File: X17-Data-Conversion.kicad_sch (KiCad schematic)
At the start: 18 parts, among them J1 Conn_01x05, SW1 1825910-6, U1 ABLS-8.000MHZ-B2-T, U2 STM32F091CCTx

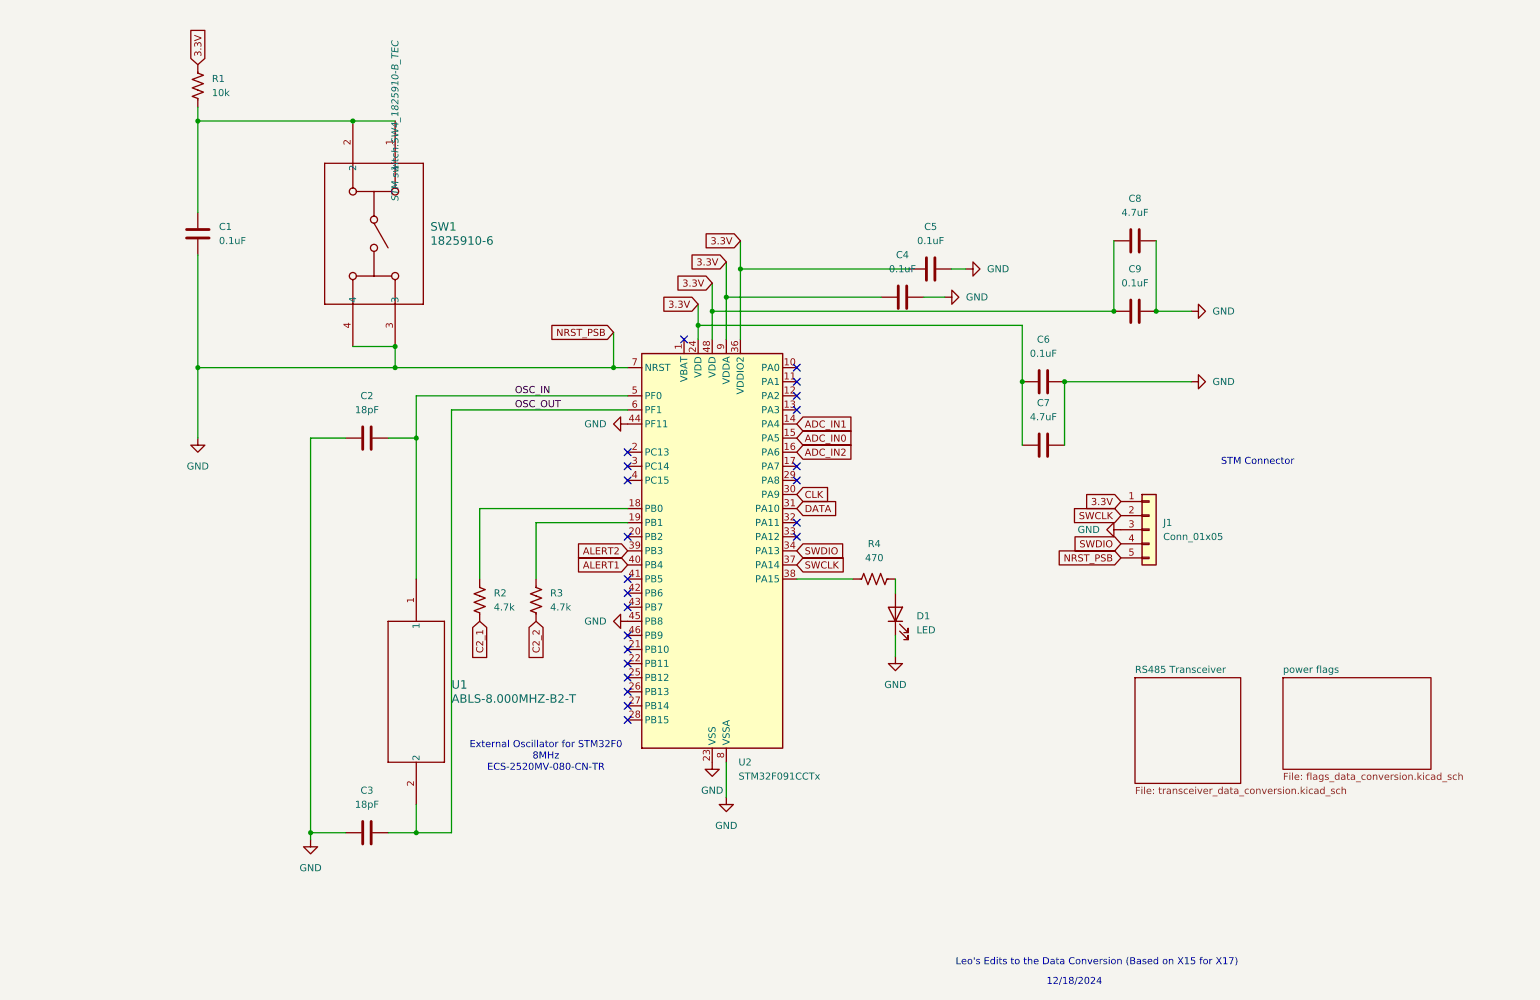
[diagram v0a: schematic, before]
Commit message: Edits part 3
Added the two new 1 by 6 vertical pin connectors to the schematic, the layout is a bit buggy tho, need to work on that next.
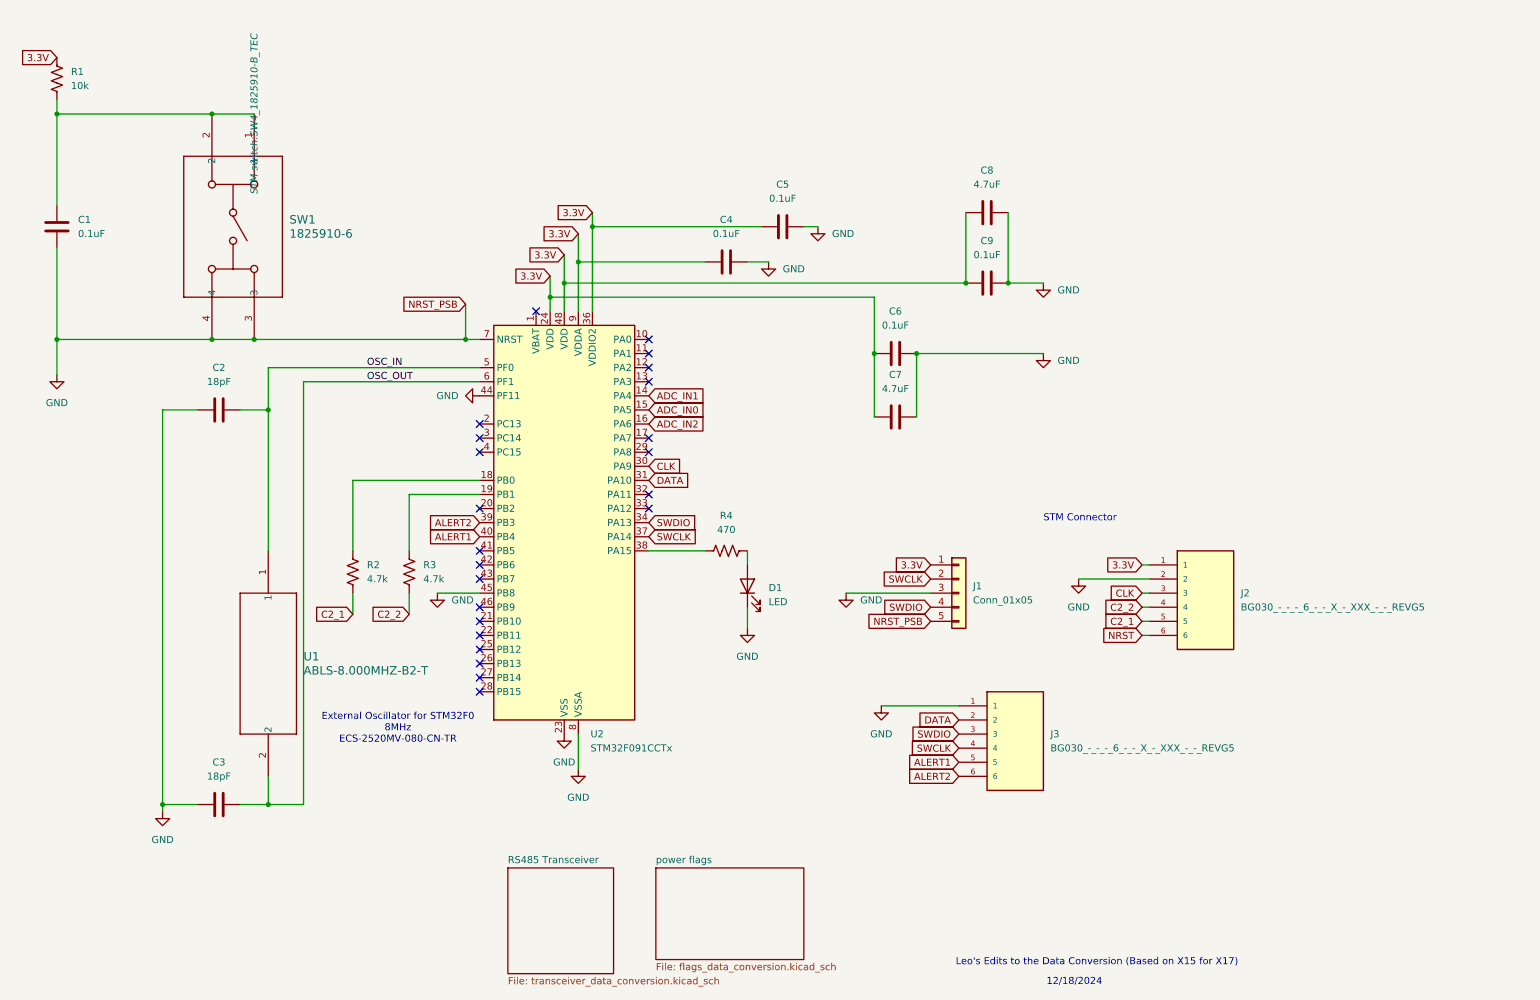
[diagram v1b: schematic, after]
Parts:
- added J2, J3: BG030_-_-_-_6_-_-_X_-_XXX_-_-_REVG5, BG030_-_-_-_6_-_-_X_-_XXX_-_-_REVG5:GCT_BG030_-_-_-_6_-_-_X_-_XXX_-_-_REVG5, symbol BG030_-_-_-_6_-_-_X_-_XXX_-_-_REVG5:BG030_-_-_-_6_-_-_X_-_XXX_-_-_REVG5
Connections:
- net 3.3V: now also J2.1
- net ALERT1: now also J3.5
- net ALERT2: now also J3.6
- net C2_1: now also J2.5
- net C2_2: now also J2.4
- net CLK: now also J2.3
- net DATA: now also J3.2
- net GND: now also J2.2, J3.1
- net SWCLK: now also J3.4
- net SWDIO: now also J3.3
- new net NRST: J2.6
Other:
- moved on the sheet: C1, C2, C3, C4, C5, C6, C7, C8, C9, D1, J1, R1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

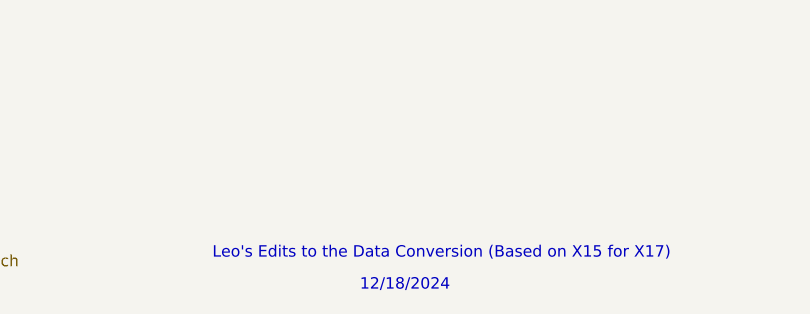
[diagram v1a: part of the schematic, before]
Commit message: Edit 4
Moved on to the layout process, then had trouble with the new connectors J2 J3 as they did not show up.
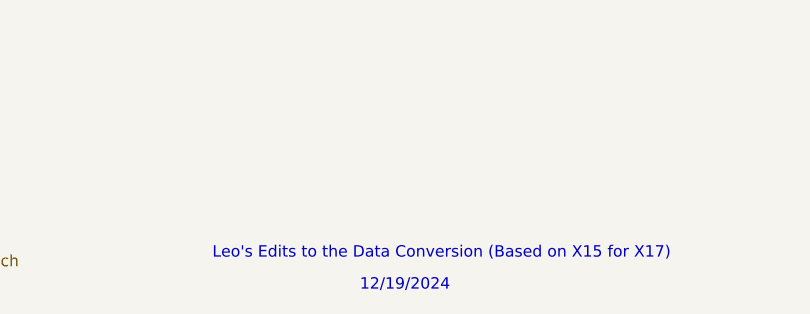
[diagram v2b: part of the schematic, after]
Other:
- note added: "12/19/2024"
- note removed: "12/18/2024"
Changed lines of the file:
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@@
 		)
 	)
-	(text "12/18/2024\n"
+	(text "12/19/2024\n"
 		(exclude_from_sim no)
 		(at 213.868 193.294 0)

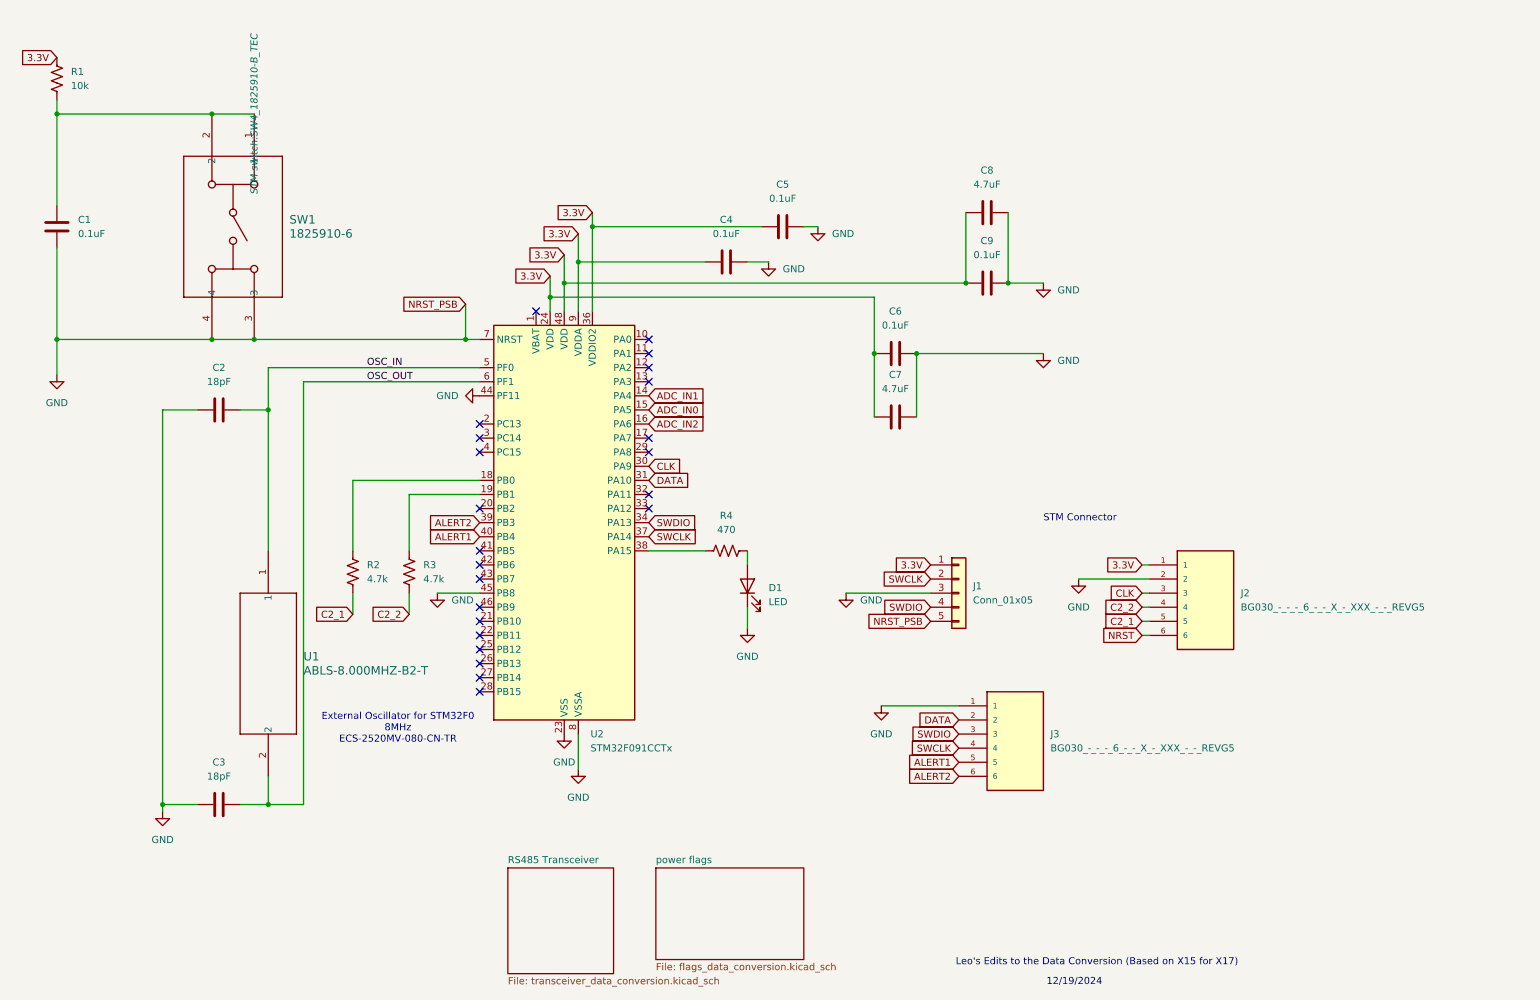
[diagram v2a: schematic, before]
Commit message: All Layout points are fixed
the layout now has all the components without errors or warnings. However, GND and NRST are all connected.
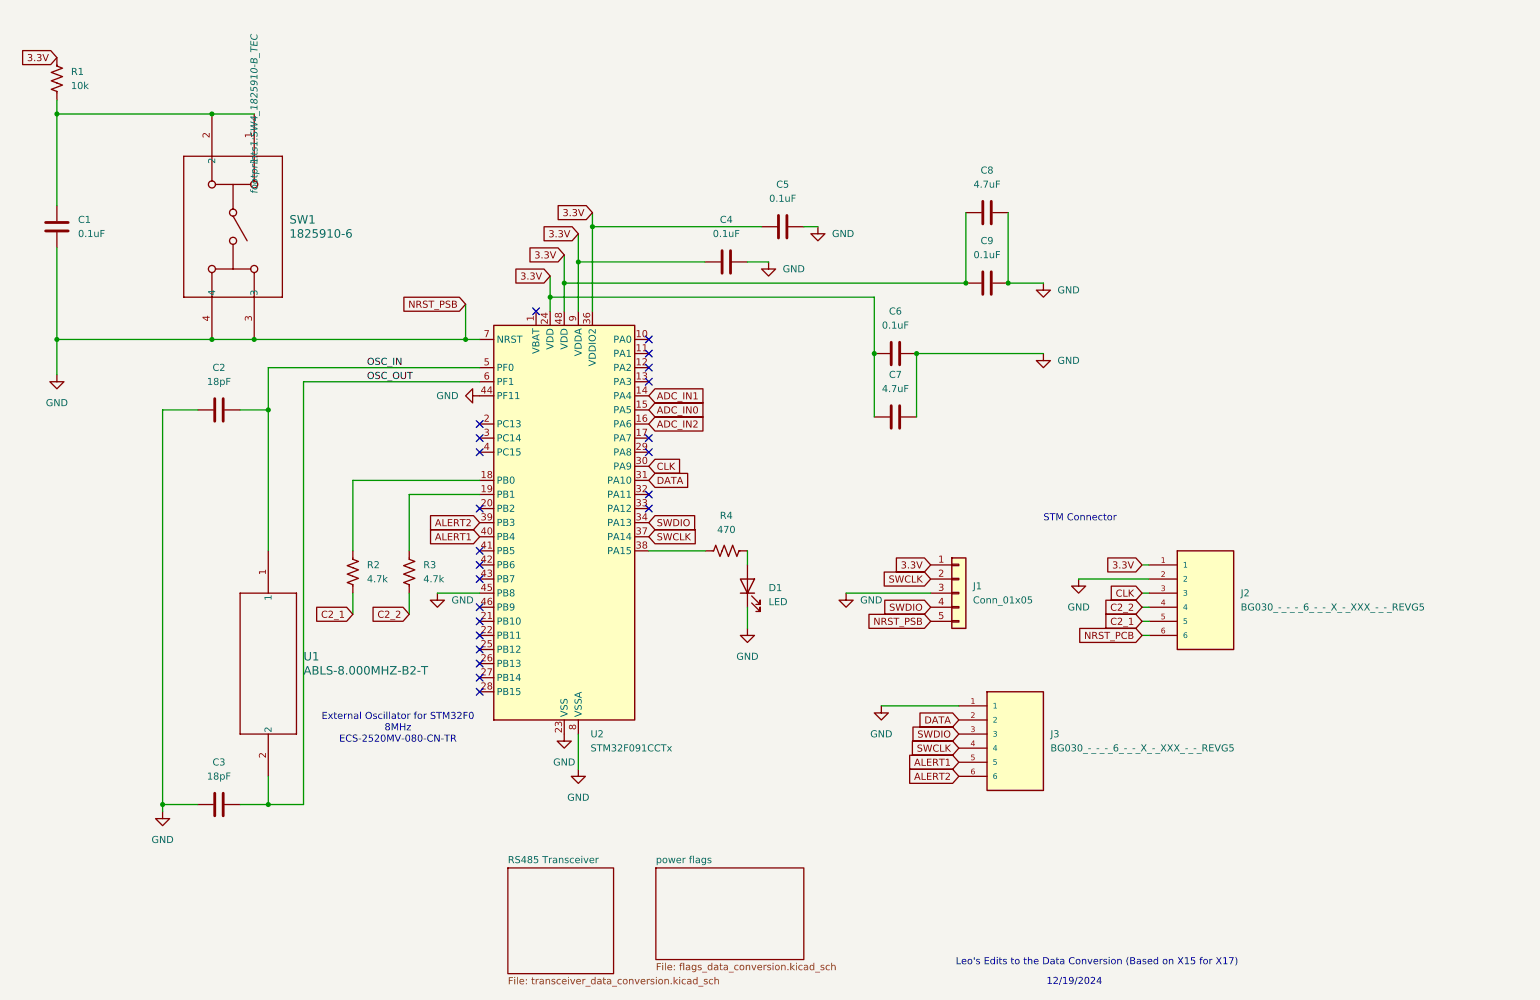
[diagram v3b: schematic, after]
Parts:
- J2, J3: footprint BG030_-_-_-_6_-_-_X_-_XXX_-_-_REVG5:GCT_BG030_-_-_-_6_-_-_X_-_XXX_-_-_REVG5 -> 61300611121:61300611121
- SW1: footprint STM switch:SW4_1825910-B_TEC -> footprints1:SW4_1825910-B_TEC
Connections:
- net NRST renamed NRST_PCB
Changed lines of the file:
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@@
 		)
 	)
-	(global_label "NRST"
+	(global_label "NRST_PCB"
 		(shape input)
 		(at 226.06 130.81 180)
@@
 		)
 		(property "Intersheetrefs" "${INTERSHEET_REFS}"
-			(at 218.2972 130.81 0)
+			(at 213.5196 130.81 0)
 			(effects
 				(font
@@
 			)
 		)
-		(property "Footprint" "BG030_-_-_-_6_-_-_X_-_XXX_-_-_REVG5:GCT_BG030_-_-_-_6_-_-_X_-_XXX_-_-_REVG5"
+		(property "Footprint" "61300611121:61300611121"
 			(at 203.2 148.59 0)
 			(effects
@@
 			)
 		)
-		(property "Footprint" "BG030_-_-_-_6_-_-_X_-_XXX_-_-_REVG5:GCT_BG030_-_-_-_6_-_-_X_-_XXX_-_-_REVG5"
+		(property "Footprint" "61300611121:61300611121"
 			(at 237.49 123.19 0)
 			(effects
@@
 			)
 		)
-		(property "Footprint" "STM switch:SW4_1825910-B_TEC"
+		(property "Footprint" "footprints1:SW4_1825910-B_TEC"
 			(at 66.04 36.83 0)
 			(effects

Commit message: Updates
Now the GND and NRST are not fully interconnected and overlapping each others signals.
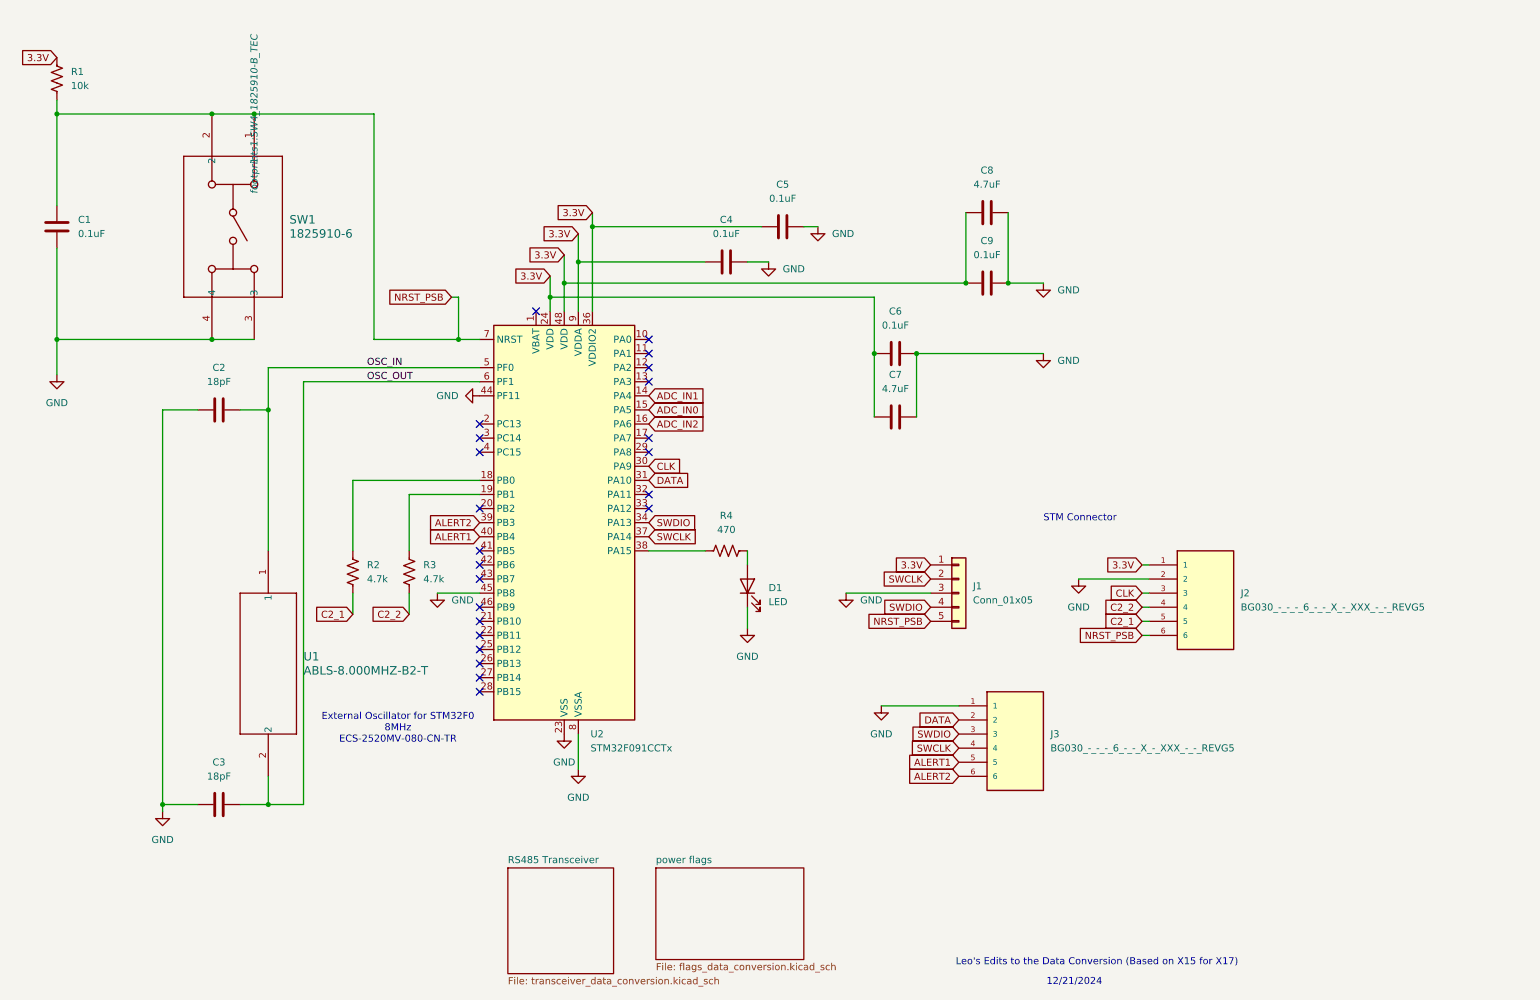
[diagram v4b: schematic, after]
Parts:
- U1: footprint footprints:ABLS-8.000MHZ-B2-T_ABR -> footprints2:ABLS-8.000MHZ-B2-T_ABR
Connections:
- net NRST_PCB is gone; now on net NRST_PSB: J2.6
- net GND: no longer J1.5 (Pin_5), U2.7 (NRST)
- net NRST_PSB: now reaches C1.1, R1.2, SW1.1, SW1.2
- net NRST_PSB: now also J1.5 (Pin_5), U2.7 (NRST)
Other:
- note added: "12/21/2024"
- note removed: "12/19/2024"
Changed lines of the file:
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@@
 	(paper "A4")
 	(junction
-		(at 66.04 77.47)
+		(at 30.48 36.83)
 		(diameter 0)
 		(color 0 0 0 0)
 	)
 	(junction
-		(at 30.48 36.83)
+		(at 49.53 161.29)
 		(diameter 0)
 		(color 0 0 0 0)
 	)
 	(junction
-		(at 49.53 161.29)
+		(at 66.04 36.83)
 		(diameter 0)
 		(color 0 0 0 0)
@@
 	)
 	(junction
-		(at 104.14 77.47)
+		(at 102.87 77.47)
 		(diameter 0)
 		(color 0 0 0 0)
@@
 	(wire
 		(pts
-			(xy 104.14 77.47) (xy 106.68 77.47)
-		)
-		(stroke
-			(width 0)
-			(type default)
-		)
-	)
-	(wire
-		(pts
 			(xy 119.38 69.85) (xy 119.38 66.04)
 		)
@@
 	(wire
 		(pts
-			(xy 104.14 71.12) (xy 104.14 77.47)
+			(xy 30.48 77.47) (xy 58.42 77.47)
 		)
 		(stroke
@@
 	(wire
 		(pts
-			(xy 30.48 77.47) (xy 58.42 77.47)
+			(xy 30.48 77.47) (xy 30.48 83.82)
 		)
 		(stroke
@@
 	(wire
 		(pts
-			(xy 30.48 77.47) (xy 30.48 83.82)
+			(xy 83.82 127) (xy 83.82 123.19)
 		)
 		(stroke
@@
 	(wire
 		(pts
-			(xy 83.82 127) (xy 83.82 123.19)
+			(xy 49.53 162.56) (xy 49.53 161.29)
 		)
 		(stroke
@@
 	(wire
 		(pts
-			(xy 49.53 162.56) (xy 49.53 161.29)
+			(xy 87.63 77.47) (xy 87.63 36.83)
 		)
 		(stroke
@@
 	(wire
 		(pts
+			(xy 102.87 69.85) (xy 102.87 77.47)
+		)
+		(stroke
+			(width 0)
+			(type default)
+		)
+	)
+	(wire
+		(pts
 			(xy 154.94 125.73) (xy 154.94 129.54)
 		)
@@
 	(wire
 		(pts
+			(xy 102.87 77.47) (xy 106.68 77.47)
+		)
+		(stroke
+			(width 0)
+			(type default)
+		)
+	)
+	(wire
+		(pts
 			(xy 68.58 161.29) (xy 74.93 161.29)
 		)
@@
 	(wire
 		(pts
-			(xy 66.04 77.47) (xy 104.14 77.47)
+			(xy 87.63 77.47) (xy 102.87 77.47)
 		)
 		(stroke
@@
 	(wire
 		(pts
+			(xy 101.6 69.85) (xy 102.87 69.85)
+		)
+		(stroke
+			(width 0)
+			(type default)
+		)
+	)
+	(wire
+		(pts
 			(xy 127 57.15) (xy 127 54.61)
 		)
@@
 	(wire
 		(pts
+			(xy 87.63 36.83) (xy 66.04 36.83)
+		)
+		(stroke
+			(width 0)
+			(type default)
+		)
+	)
+	(wire
+		(pts
 			(xy 119.38 69.85) (xy 177.8 69.85)
 		)
@@
 		)
 	)
-	(text "12/19/2024\n"
+	(text "12/21/2024\n"
 		(exclude_from_sim no)
 		(at 213.868 193.294 0)
@@
 	(global_label "NRST_PSB"
 		(shape input)
-		(at 104.14 71.12 180)
+		(at 101.6 69.85 180)
 		(fields_autoplaced yes)
 		(effects
@@
 		)
 		(property "Intersheetrefs" "${INTERSHEET_REFS}"
-			(at 91.6601 71.12 0)
+			(at 89.1201 69.85 0)
 			(effects
 				(font
@@
 		)
 	)
-	(global_label "NRST_PCB"
+	(global_label "NRST_PSB"
 		(shape input)
 		(at 226.06 130.81 180)
@@
 		)
 		(property "Intersheetrefs" "${INTERSHEET_REFS}"
-			(at 213.5196 130.81 0)
+			(at 213.5801 130.81 0)
 			(effects
 				(font
@@
 			)
 		)
-		(property "Footprint" "footprints:ABLS-8.000MHZ-B2-T_ABR"
+		(property "Footprint" "footprints2:ABLS-8.000MHZ-B2-T_ABR"
 			(at 68.58 115.57 0)
 			(effects
